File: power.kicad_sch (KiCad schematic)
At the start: 17 parts, among them SW1 SW_Push, SW2 SW_Push, U3 AMS1117-3.3

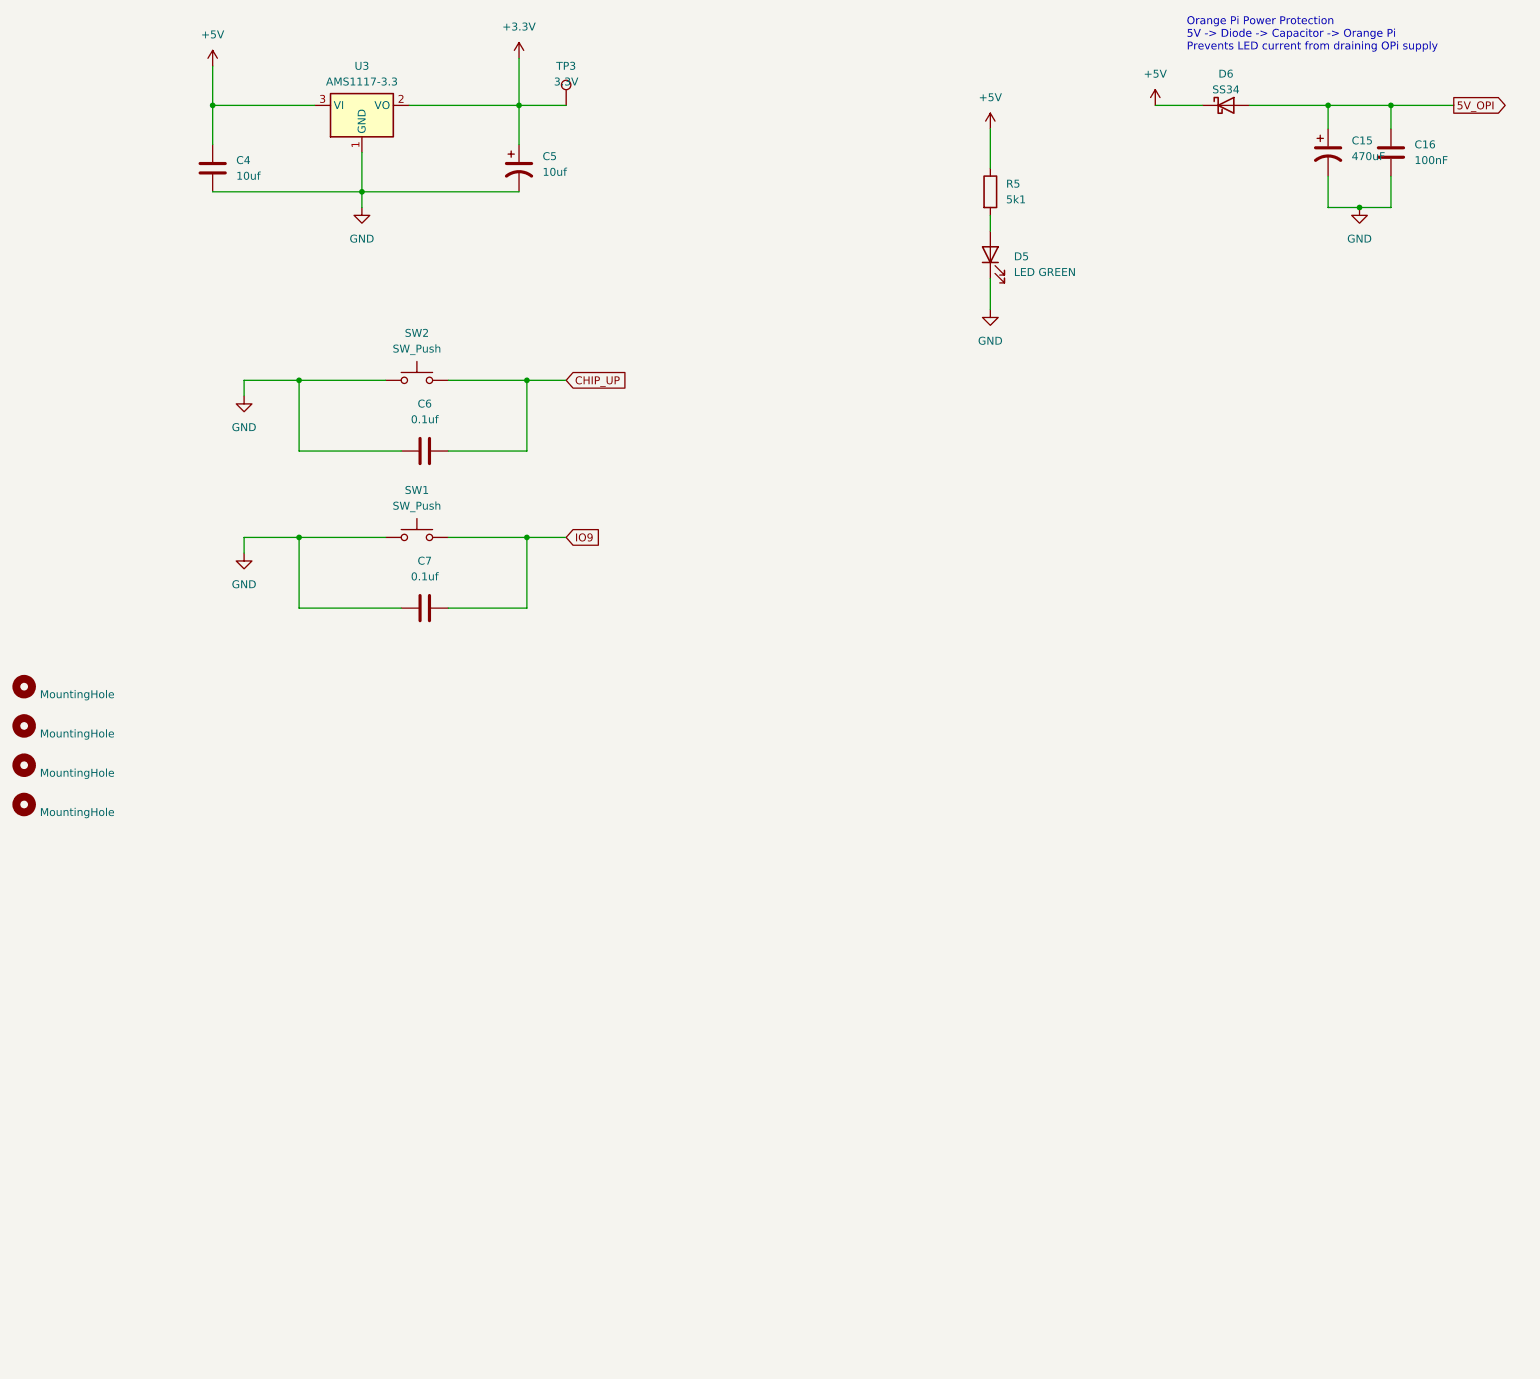
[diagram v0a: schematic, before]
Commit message: Rework v4 schematic for Raspberry Pi 4/5 HAT
- Remap J1 to the Raspberry Pi 40-pin pinout (was still Orange Pi pin
  numbers: Pi 3V3 on MISO, GND on ESP32 RX)
- Fix auto-reset: U4 collectors drove EN and IO9 the wrong way round
- Let the Pi flash the ESP32: UART via 74LVC1G08 AND gate (U10) shared
  with the CP2102N, EN/BOOT on GPIO5/6 through 1k; add IO9 pull-up
- Power the Pi straight from +5V, drop the SS34 diode (D6)
- Add fan control: AO3400A low-side switch on GPIO18, tach on GPIO24
- Move mux LEDs D1-D3 off strapping pin GPIO8 to the 5V select lines
- Add 3V3 power LED and test points TP8-TP33
- Document v4 in CLAUDE.md

Co-Authored-By: Claude Opus 5.5 <noreply@anthropic.com>
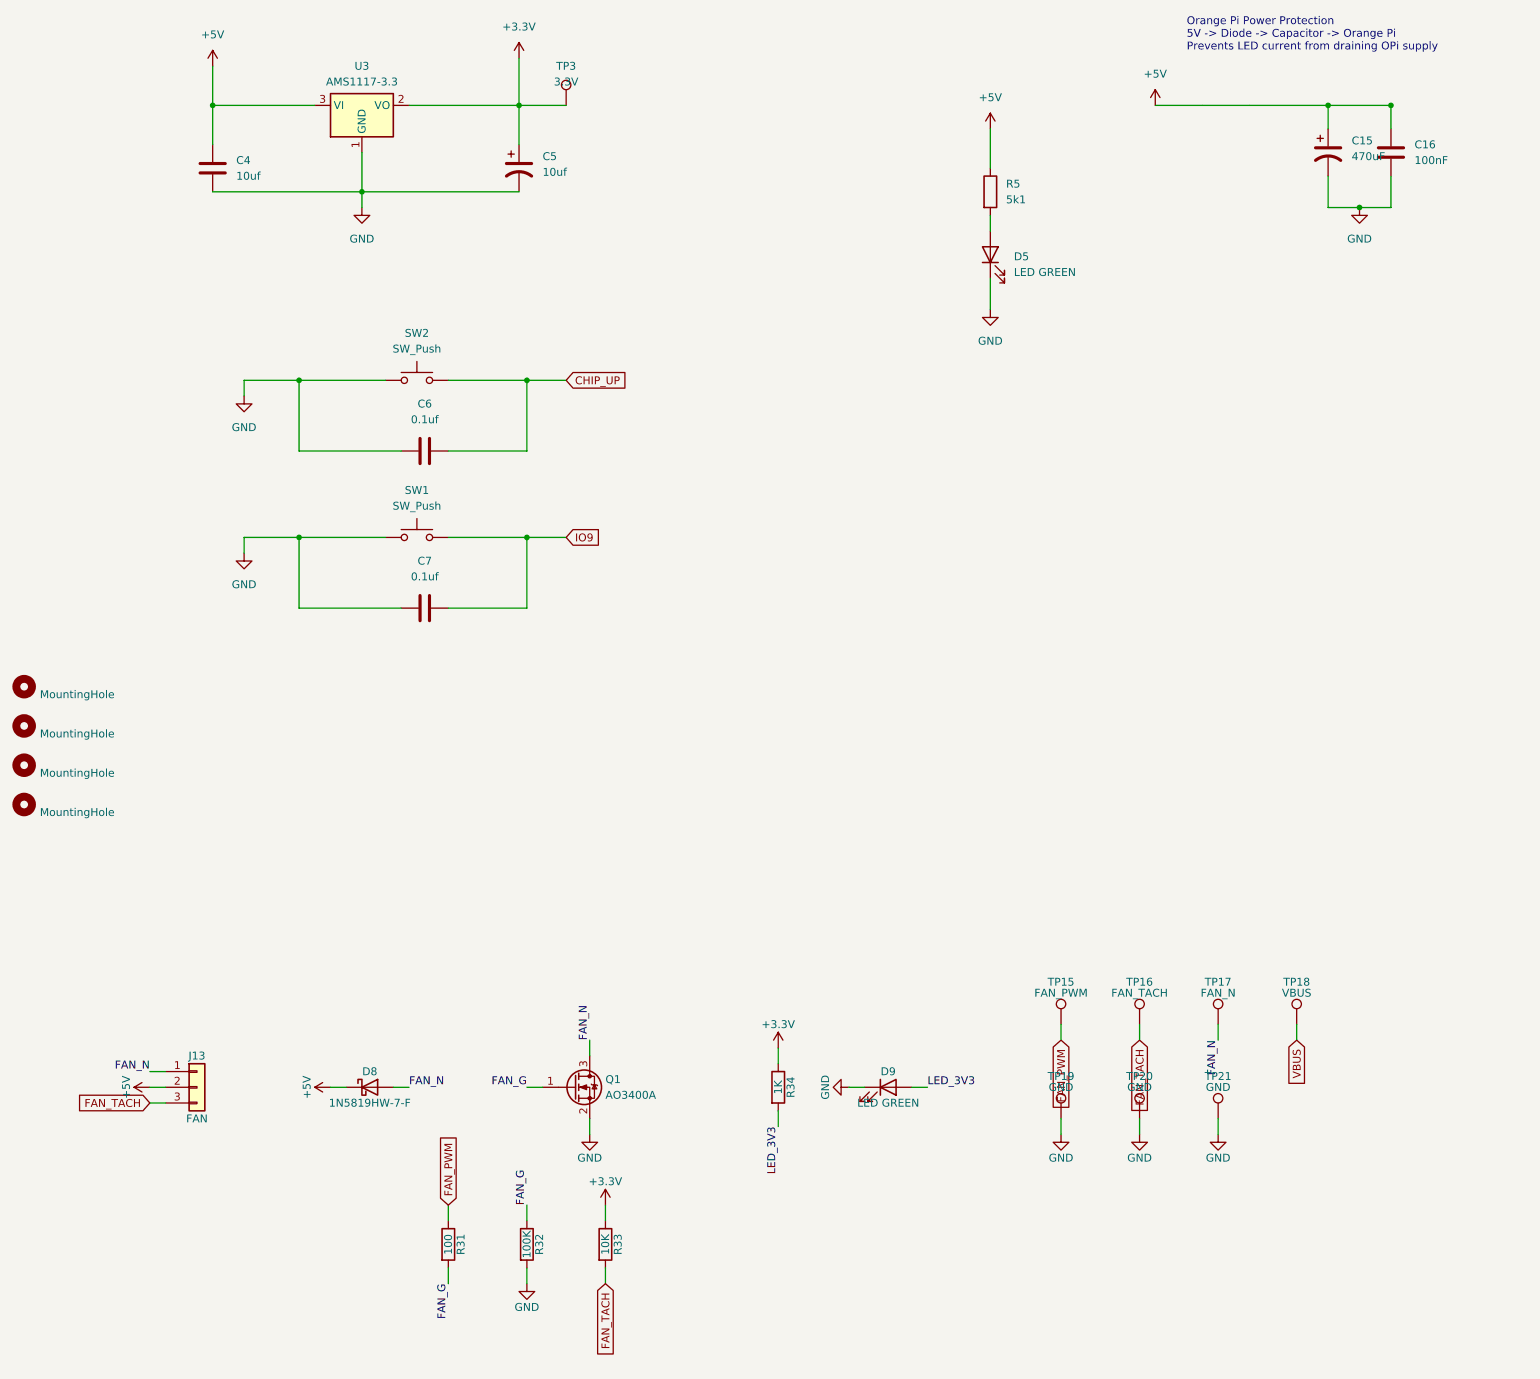
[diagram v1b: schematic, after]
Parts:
- removed D6: SS34, Diode_SMD:D_SMC, symbol Device:D_Schottky
- added D8: 1N5819HW-7-F, Diode_SMD:D_SOD-123, symbol Device:D_Schottky
- added D9: LED GREEN, LED_SMD:LED_0805_2012Metric, symbol Device:LED
- added J13: FAN, Connector_PinHeader_2.54mm:PinHeader_1x03_P2.54mm_Vertical, symbol Connector_Generic:Conn_01x03
- added Q1: AO3400A, Package_TO_SOT_SMD:SOT-23, symbol Device:Q_NMOS_GSD
- added R31: 100, Resistor_SMD:R_0603_1608Metric, symbol Device:R
- added R32: 100K, Resistor_SMD:R_0603_1608Metric, symbol Device:R
- added R33: 10K, Resistor_SMD:R_0603_1608Metric, symbol Device:R
- added R34: 1K, Resistor_SMD:R_0603_1608Metric, symbol Device:R
- added TP15: FAN_PWM, TestPoint:TestPoint_Pad_1.0x1.0mm, symbol Connector:TestPoint
- added TP16: FAN_TACH, TestPoint:TestPoint_Pad_1.0x1.0mm, symbol Connector:TestPoint
- added TP17: FAN_N, TestPoint:TestPoint_Pad_1.0x1.0mm, symbol Connector:TestPoint
- added TP18: VBUS, TestPoint:TestPoint_Pad_1.0x1.0mm, symbol Connector:TestPoint
- added TP19, TP20, TP21: GND, TestPoint:TestPoint_Pad_1.0x1.0mm, symbol Connector:TestPoint
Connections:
- net 5V_OPI is gone; now on net +5V: C15.1, C16.1
- net +3.3V: now also R33.1, R34.1
- net +5V: now also D8.1 (K), J13.2 (Pin_2)
- net GND: now also D9.1 (K), Q1.2 (S), R32.2, TP19.1, TP20.1, TP21.1
- new net FAN_G: Q1.1 (G), R31.2, R32.1
- new net FAN_N: D8.2 (A), J13.1 (Pin_1), Q1.3 (D), TP17.1
- new net FAN_PWM: R31.1, TP15.1
- new net FAN_TACH: J13.3 (Pin_3), R33.2, TP16.1
- new net LED_3V3: D9.2 (A), R34.2
- new net VBUS: TP18.1

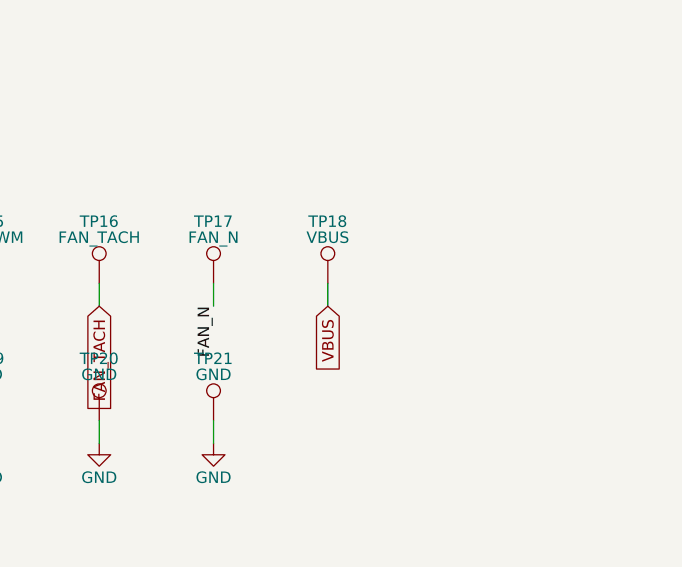
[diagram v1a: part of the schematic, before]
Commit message: Add first v4 HAT layout (4 layers, autorouted draft)
- 65x56 mm Raspberry Pi HAT outline, J1 on the bottom at the Pi position
- 4 layers: signal + GND pour on outer layers, In1 GND plane, In2 +5V plane,
  GND stitching vias
- Locked wide power tracks from the screw terminals to the JST outputs and
  to the Pi 5V pins; net classes for power and 3V3
- Address LEDs D1-D3 in one row, power LEDs next to the power input
- Autorouted with Freerouting; 8 connections, 3 edge clearances and the
  silkscreen still need hand work
- Add PWR_FLAG to +5V and GND, remove a stray no-connect (ERC clean)

Co-Authored-By: Claude Opus 5.5 <noreply@anthropic.com>
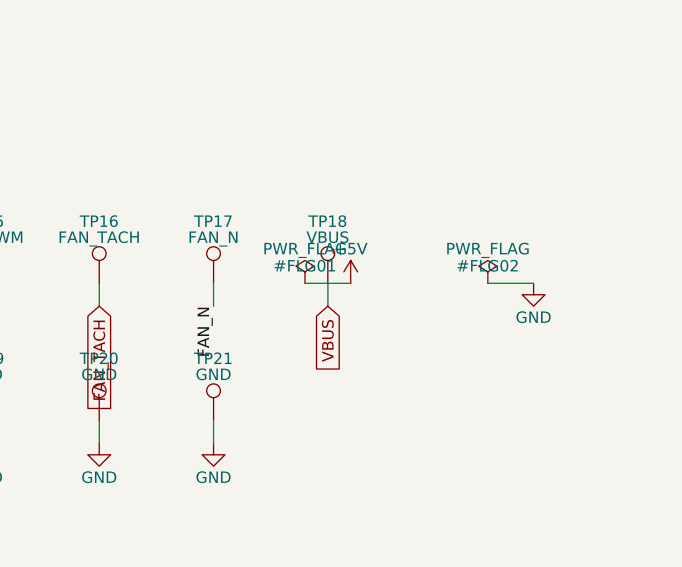
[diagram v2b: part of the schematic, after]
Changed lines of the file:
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@@
+    )
+  )
+  (symbol (lib_id "power:PWR_FLAG") (at 236.22 190.5 0) (unit 1)
+    (in_bom no) (on_board no) (dnp no)
+    (property "Reference" "#FLG01" (at 236.22 188.595 0)
+      (effects (font (size 1.27 1.27) ) )
+    )
+    (property "Value" "PWR_FLAG" (at 236.22 186.69 0)
+      (effects (font (size 1.27 1.27) ) )
+    )
+    (property "Footprint" "" (at 236.22 190.5 0)
+      (effects (font (size 1.27 1.27) )  hide)
+    )
+    (property "Datasheet" "" (at 236.22 190.5 0)
+      (effects (font (size 1.27 1.27) )  hide)
+    )
+    (pin "1")
+    (instances
+      (project "Julelys"
+        (path "/9ef41b73-8dcb-4021-8930-5b1db22eb182/75d2635a-f2eb-4079-86f3-082e38564c79"
+          (reference "#FLG01") (unit 1)
+        )
+      )
+    )
+  )
+  (wire (pts (xy 236.22 190.5) (xy 241.3 190.5))
+    (stroke (width 0) (type default))
+  )
+  (symbol (lib_id "power:+5V") (at 241.3 190.5 0) (unit 1)
+    (in_bom yes) (on_board yes) (dnp no) (fields_autoplaced)
+    (property "Reference" "#PWR0201" (at 241.3 190.5 0)
+      (effects (font (size 1.27 1.27)) hide)
+    )
+    (property "Value" "+5V" (at 241.3 186.69 0)
+      (effects (font (size 1.27 1.27)))
+    )
+    (property "Footprint" "" (at 241.3 190.5 0)
+      (effects (font (size 1.27 1.27)) hide)
+    )
+    (property "Datasheet" "" (at 241.3 190.5 0)
+      (effects (font (size 1.27 1.27)) hide)
+    )
+    (pin "1")
+    (instances
+      (project "Julelys"
+        (path "/9ef41b73-8dcb-4021-8930-5b1db22eb182/75d2635a-f2eb-4079-86f3-082e38564c79"
+          (reference "#PWR0201") (unit 1)
+        )
+      )
+    )
+  )
+  (symbol (lib_id "power:PWR_FLAG") (at 256.54 190.5 0) (unit 1)
+    (in_bom no) (on_board no) (dnp no)
+    (property "Reference" "#FLG02" (at 256.54 188.595 0)
+      (effects (font (size 1.27 1.27) ) )
+    )
+    (property "Value" "PWR_FLAG" (at 256.54 186.69 0)
+      (effects (font (size 1.27 1.27) ) )
+    )
+    (property "Footprint" "" (at 256.54 190.5 0)
+      (effects (font (size 1.27 1.27) )  hide)
+    )
+    (property "Datasheet" "" (at 256.54 190.5 0)
+      (effects (font (size 1.27 1.27) )  hide)
+    )
+    (pin "1")
+    (instances
+      (project "Julelys"
+        (path "/9ef41b73-8dcb-4021-8930-5b1db22eb182/75d2635a-f2eb-4079-86f3-082e38564c79"
+          (reference "#FLG02") (unit 1)
+        )
+      )
+    )
+  )
+  (wire (pts (xy 256.54 190.5) (xy 261.62 190.5))
+    (stroke (width 0) (type default))
+  )
+  (symbol (lib_id "power:GND") (at 261.62 190.5 0) (unit 1)
+    (in_bom yes) (on_board yes) (dnp no) (fields_autoplaced)
+    (property "Reference" "#PWR0202" (at 261.62 190.5 0)
+      (effects (font (size 1.27 1.27)) hide)
+    )
+    (property "Value" "GND" (at 261.62 194.31 0)
+      (effects (font (size 1.27 1.27)))
+    )
+    (property "Footprint" "" (at 261.62 190.5 0)
+      (effects (font (size 1.27 1.27)) hide)
+    )
+    (property "Datasheet" "" (at 261.62 190.5 0)
+      (effects (font (size 1.27 1.27)) hide)
+    )
+    (pin "1")
+    (instances
+      (project "Julelys"
+        (path "/9ef41b73-8dcb-4021-8930-5b1db22eb182/75d2635a-f2eb-4079-86f3-082e38564c79"
+          (reference "#PWR0202") (unit 1)
+        )
+      )
     )
   )

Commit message: Match the official HAT mounting hole spec
- Mounting holes 2.75 mm NPTH (was 3.2 mm M3), footprint
  MountingHole_2.7mm_M2.5 in board and schematic
- 6.4 mm copper/track/via keepout around each hole on all layers
  (spec: land min 6.2 mm, not connected to GND)
- Drop the 1 mm Pi 5V track around the left end of J1, which crossed the
  hole land; pins 2/4 are fed by the In2 +5V plane
- Reroute FAN_PWM and CH3 around the top-right hole land
- Document the HAT mechanical spec (65 x 56.0 mm for a THT header)

Co-Authored-By: Claude Opus 5.5 <noreply@anthropic.com>
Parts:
- H1, H2, H3, H4: footprint MountingHole:MountingHole_3.2mm_M3 -> MountingHole:MountingHole_2.7mm_M2.5
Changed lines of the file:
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@@
       (effects (font (size 1.27 1.27)) (justify left))
     )
-    (property "Footprint" "MountingHole:MountingHole_3.2mm_M3" (at 33.02 135.89 0)
+    (property "Footprint" "MountingHole:MountingHole_2.7mm_M2.5" (at 33.02 135.89 0)
       (effects (font (size 1.27 1.27)) hide)
     )
@@
       (effects (font (size 1.27 1.27)) (justify left))
     )
-    (property "Footprint" "MountingHole:MountingHole_3.2mm_M3" (at 33.02 142.24 0)
+    (property "Footprint" "MountingHole:MountingHole_2.7mm_M2.5" (at 33.02 142.24 0)
       (effects (font (size 1.27 1.27)) hide)
     )
@@
       (effects (font (size 1.27 1.27)) (justify left))
     )
-    (property "Footprint" "MountingHole:MountingHole_3.2mm_M3" (at 33.02 154.94 0)
+    (property "Footprint" "MountingHole:MountingHole_2.7mm_M2.5" (at 33.02 154.94 0)
       (effects (font (size 1.27 1.27)) hide)
     )
@@
       (effects (font (size 1.27 1.27)) (justify left))
     )
-    (property "Footprint" "MountingHole:MountingHole_3.2mm_M3" (at 33.02 148.59 0)
-      (effects (font (size 1.27 1.27)) hide)
-    )
+    (property "Footprint" "MountingHole:MountingHole_2.7mm_M2.5" (at 33.02 148.59 0)
+      (effects (font (size 1.27 1.27)) hide)
+    )

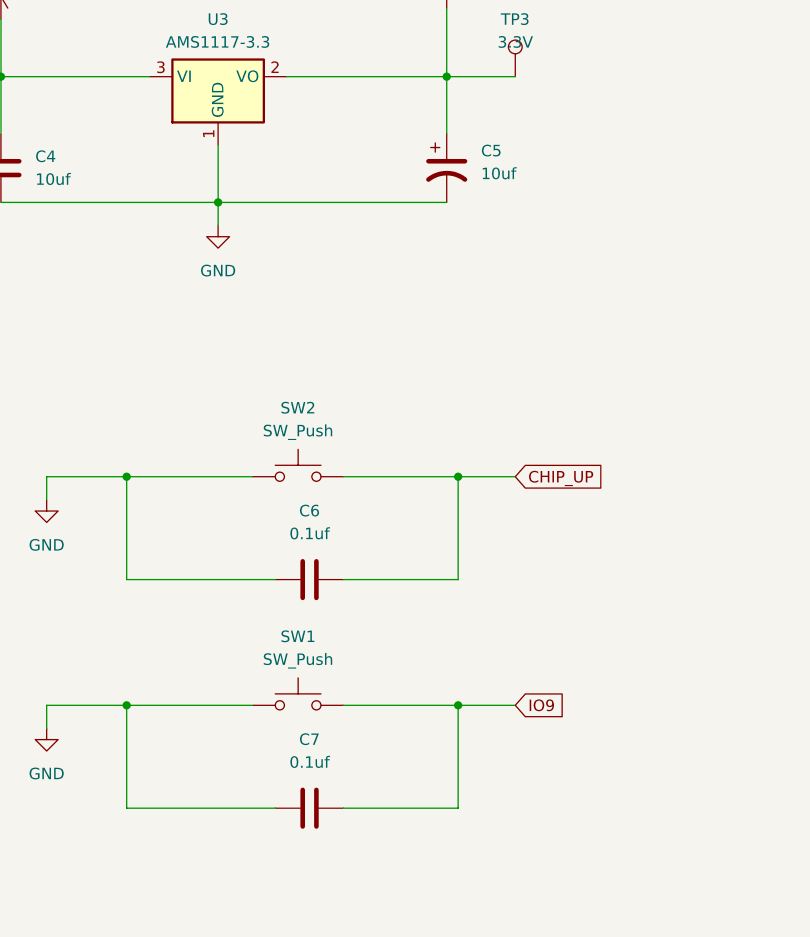
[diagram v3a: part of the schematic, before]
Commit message: Apply schematic review fixes, add JLCPCB rules, prepare for manual layout
Schematic (from a Codex review):
- R35 10k pull-up on GPIO2 (strapping pin; Pi MISO has a default pull-down)
- R36 10k pull-down on IO7 so the LEDs stay dark while the ESP32 boots
- C5 22uF for AMS1117 output stability, C7 1nF on GPIO9
- C18-C21 100nF decoupling for the level shifters U6-U9

Board:
- New parts parked outside the outline for manual placement
- Silkscreen scaled to JLCPCB's 1.0 mm minimum; back pinout table rebuilt
- C5/C7 values synced

Rules:
- JLCPCB 4-layer limits in Julelys.kicad_pro and new Julelys.kicad_dru

Co-Authored-By: Claude Opus 5.5 <noreply@anthropic.com>
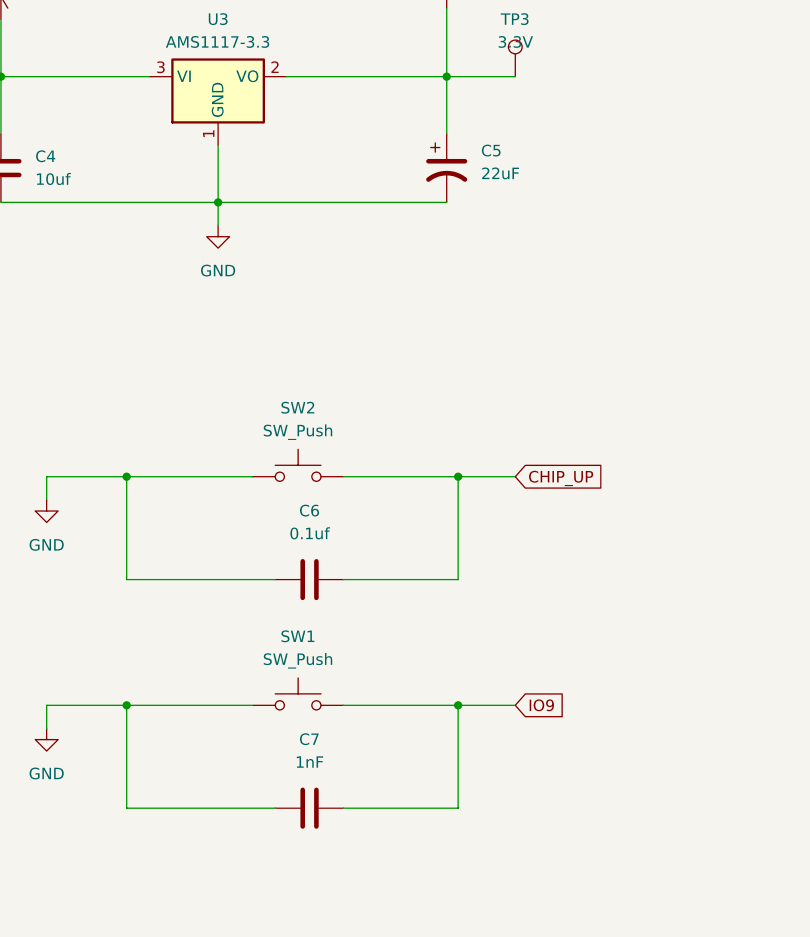
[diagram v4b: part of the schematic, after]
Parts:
- C5: value 10uf -> 22uF
- C7: value 0.1uf -> 1nF
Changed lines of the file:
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@@
       (effects (font (size 1.27 1.27)) (justify left))
     )
-    (property "Value" "10uf" (at 116.84 52.705 0)
+    (property "Value" "22uF" (at 116.84 52.705 0)
       (effects (font (size 1.27 1.27)) (justify left))
     )
@@
       (effects (font (size 1.27 1.27)))
     )
-    (property "Value" "0.1uf" (at 97.79 118.11 90)
-      (effects (font (size 1.27 1.27)))
-    )
+    (property "Value" "1nF" (at 97.79 118.11 90)
+      (effects (font (size 1.27 1.27)))
+    )
